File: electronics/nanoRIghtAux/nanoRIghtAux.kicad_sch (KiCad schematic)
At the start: 16 parts, among them J1 Conn_MM5451, J10 Conn_EA-GLCD, J11 Conn_MAX7219, J2 Conn_HYDA, J3 Conn_HYDB, J4 Conn_FUEL_FR, J5 Conn_FUEL_AL, J6 Conn_MOT_D, J7 Conn_MOT_C, J8 Conn_MOT_B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

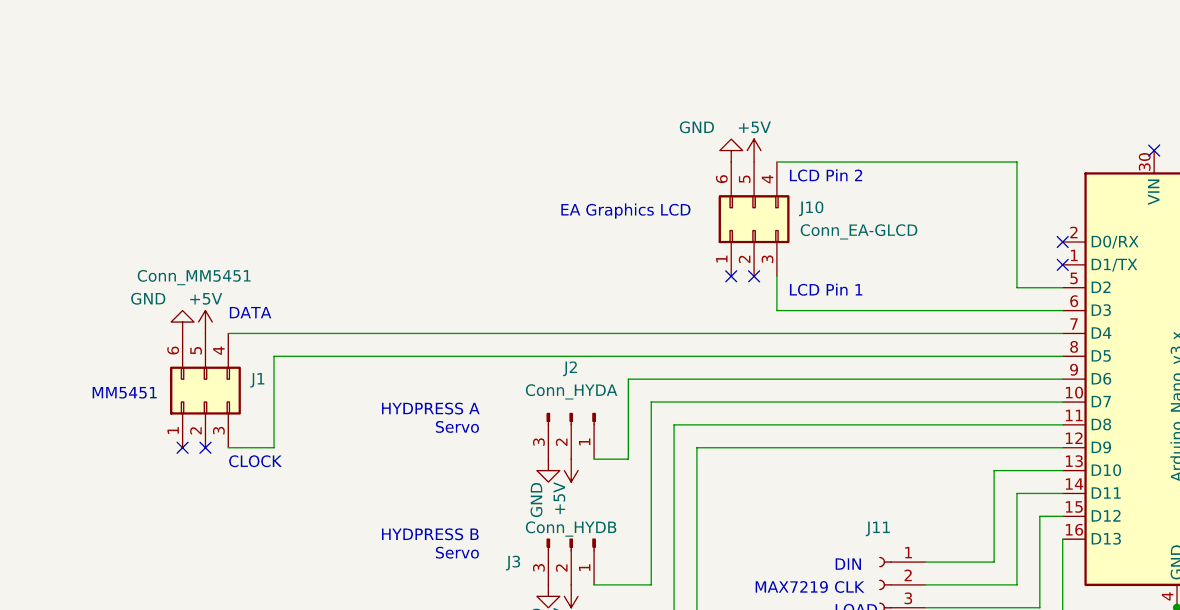
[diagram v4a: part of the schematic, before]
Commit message: changed 2x03 connector type
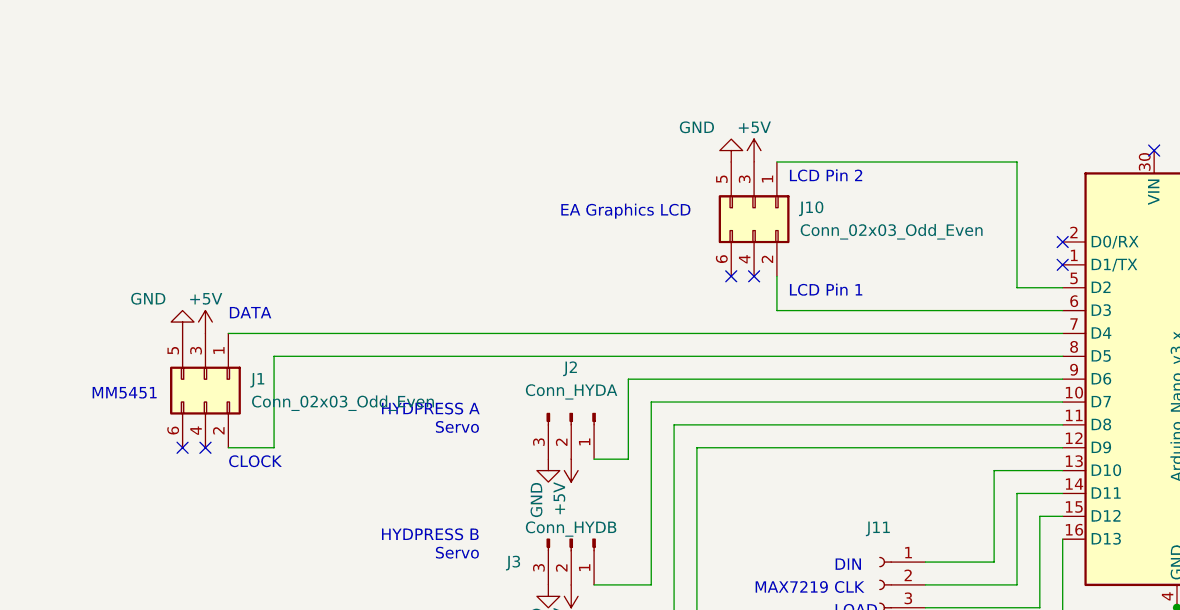
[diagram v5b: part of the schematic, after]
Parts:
- removed J1: Conn_MM5451, Connector_PinHeader_2.54mm:PinHeader_2x03_P2.54mm_Vertical, symbol Connector_Generic:Conn_02x03_Counter_Clockwise
- removed J10: Conn_EA-GLCD, Connector_PinHeader_2.54mm:PinHeader_2x03_P2.54mm_Vertical, symbol Connector_Generic:Conn_02x03_Counter_Clockwise
- added J1: Conn_02x03_Odd_Even, Connector_PinHeader_2.54mm:PinHeader_2x03_P2.54mm_Vertical, symbol Connector_Generic:Conn_02x03_Odd_Even
- added J10: Conn_02x03_Odd_Even, symbol Connector_Generic:Conn_02x03_Odd_Even
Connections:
- net +5V: now also J1.3 (Pin_3), J10.3 (Pin_3)
- net GND: now also J1.5 (Pin_5), J10.5 (Pin_5)
- net at A1.8 (D5): now also J1.2 (Pin_2)
- net at A1.7 (D4): now also J1.1 (Pin_1)
- net at A1.6 (D3): now also J10.2 (Pin_2)
- net at A1.5 (D2): now also J10.1 (Pin_1)

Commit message: PCB edit started
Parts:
- J1: value Conn_02x03_Odd_Even -> Conn_MM5451
- J10: value Conn_02x03_Odd_Even -> Conn_EA_GLCD; footprint (none) -> Connector_PinHeader_2.54mm:PinHeader_2x03_P2.54mm_Vertical
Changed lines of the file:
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@@
   )
   (symbol (lib_id "Connector_Generic:Conn_02x03_Odd_Even") (at 50.8 85.09 270) (unit 1)
-    (in_bom yes) (on_board yes) (dnp no) (fields_autoplaced)
+    (in_bom yes) (on_board yes) (dnp no)
     (property "Reference" "J1" (at 55.88 85.09 90)
       (effects (font (size 1.27 1.27)) (justify left))
     )
-    (property "Value" "Conn_02x03_Odd_Even" (at 55.88 87.63 90)
+    (property "Value" "Conn_MM5451" (at 33.02 83.82 90)
       (effects (font (size 1.27 1.27)) (justify left))
     )
@@
       (effects (font (size 1.27 1.27)) (justify left))
     )
-    (property "Value" "Conn_02x03_Odd_Even" (at 116.84 68.58 90)
+    (property "Value" "Conn_EA_GLCD" (at 116.84 68.58 90)
       (effects (font (size 1.27 1.27)) (justify left))
     )
-    (property "Footprint" "" (at 111.76 66.04 0)
+    (property "Footprint" "Connector_PinHeader_2.54mm:PinHeader_2x03_P2.54mm_Vertical" (at 111.76 66.04 0)
       (effects (font (size 1.27 1.27)) hide)
     )

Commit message: PWR input pinheader added, MAX7219_PWR pinheader added, PCB routing changed
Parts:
- added J12: Conn_PWRInput, Connector_PinHeader_2.54mm:PinHeader_1x02_P2.54mm_Vertical, symbol Connector:Conn_01x02_Pin
- added J13: Conn_MAX_Pwr, Connector_PinSocket_2.54mm:PinSocket_1x02_P2.54mm_Vertical, symbol Connector:Conn_01x02_Socket
- SW1, SW2, SW3: footprint Button_Switch_THT:SW_PUSH_6mm -> Connector_PinHeader_2.54mm:PinHeader_1x02_P2.54mm_Vertical
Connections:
- net +5V: now also J12.2 (Pin_2), J13.2 (Pin_2)
- net GND: now also J12.1 (Pin_1), J13.1 (Pin_1)
- net at J6.3 (Pin_3): now also U3.10 (Mot_D4); no longer U3.11 (Mot_D3)
- net at J6.4 (Pin_4): now also U3.11 (Mot_D3); no longer U3.10 (Mot_D4)
- net at J8.3 (Pin_3): now also U3.24 (Mot_B4); no longer U3.25 (Mot_B3)
- net at J8.4 (Pin_4): now also U3.25 (Mot_B3); no longer U3.24 (Mot_B4)
- net at J7.3 (Pin_3): now also U3.19 (Mot_C4); no longer U3.18 (Mot_C3)
- net at J7.4 (Pin_4): now also U3.18 (Mot_C3); no longer U3.19 (Mot_C4)
- net at J9.3 (Pin_3): now also U3.5 (Mot_A4); no longer U3.4 (Mot_A3)
- net at J9.4 (Pin_4): now also U3.4 (Mot_A3); no longer U3.5 (Mot_A4)
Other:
- moved on the sheet: J6, J7, J8, J9

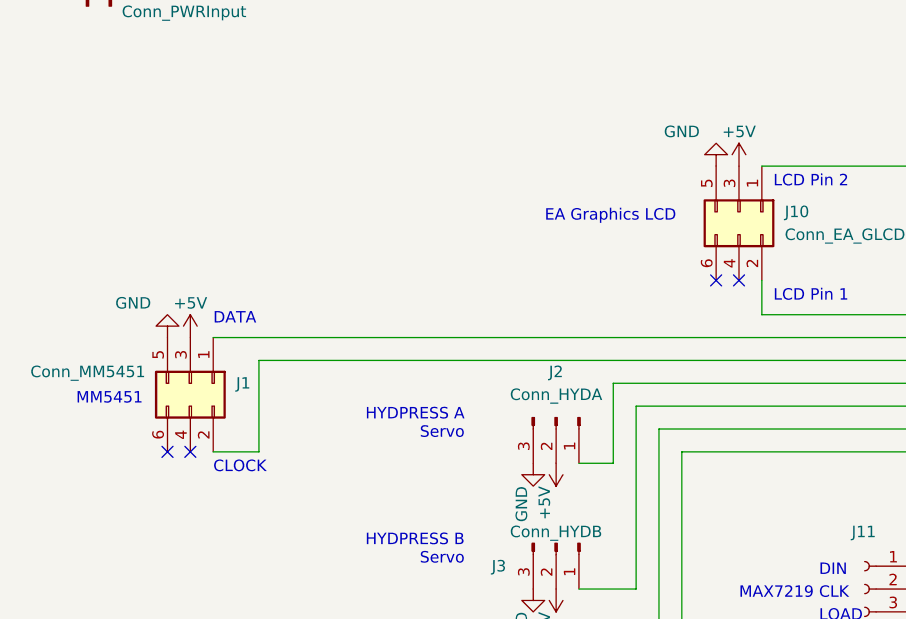
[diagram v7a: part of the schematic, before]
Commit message: first routing of TH components done.
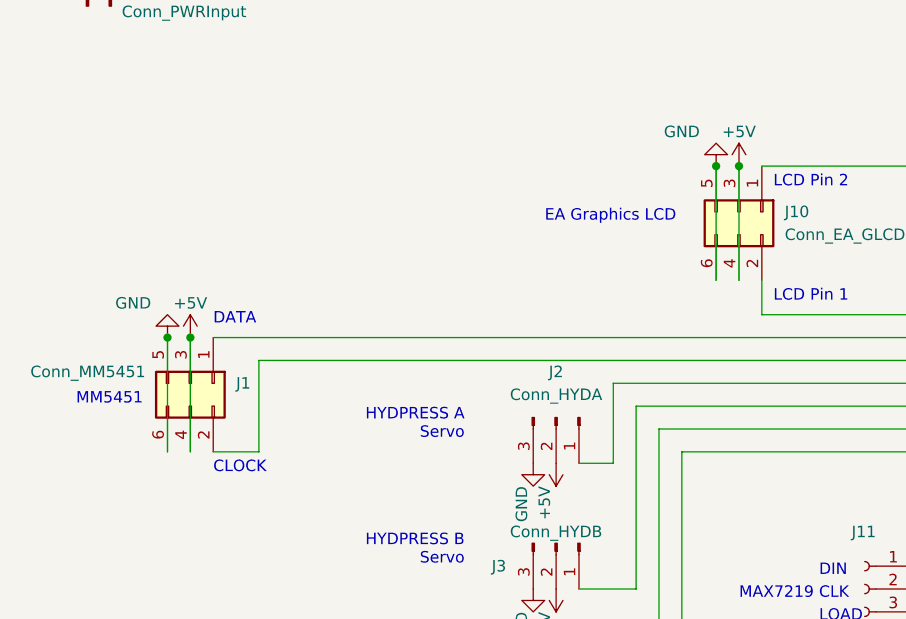
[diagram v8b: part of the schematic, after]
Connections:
- net +5V: now also J1.4 (Pin_4), J10.4 (Pin_4)
- net GND: now also J1.6 (Pin_6), J10.6 (Pin_6)
- no-connect marks 13 -> 9
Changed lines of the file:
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@@
   (junction (at 177.8 124.46) (diameter 0) (color 0 0 0 0)
   )
+  (junction (at 48.26 80.01) (diameter 0) (color 0 0 0 0)
+  )
   (junction (at 46.99 26.67) (diameter 0) (color 0 0 0 0)
   )
+  (junction (at 111.76 60.96) (diameter 0) (color 0 0 0 0)
+  )
+  (junction (at 50.8 80.01) (diameter 0) (color 0 0 0 0)
+  )
   (junction (at 158.75 110.49) (diameter 0) (color 0 0 0 0)
   )
   (junction (at 35.56 26.67) (diameter 0) (color 0 0 0 0)
   )
-  (no_connect (at 50.8 92.71))
+  (junction (at 109.22 60.96) (diameter 0) (color 0 0 0 0)
+  )
   (no_connect (at 163.83 59.69))
   (no_connect (at 156.21 59.69))
-  (no_connect (at 48.26 92.71))
   (no_connect (at 161.29 59.69))
   (no_connect (at 146.05 69.85))
-  (no_connect (at 109.22 73.66))
   (no_connect (at 171.45 80.01))
   (no_connect (at 146.05 72.39))
-  (no_connect (at 111.76 73.66))
   (no_connect (at 207.01 76.2))
   (no_connect (at 207.01 73.66))
@@
     (stroke (width 0) (type default))
   )
+  (wire (pts (xy 50.8 80.01) (xy 50.8 92.71))
+    (stroke (width 0) (type default))
+  )
   (wire (pts (xy 102.87 121.92) (xy 92.71 121.92))
     (stroke (width 0) (type default))
@@
     (stroke (width 0) (type default))
   )
+  (wire (pts (xy 48.26 80.01) (xy 48.26 92.71))
+    (stroke (width 0) (type default))
+  )
   (wire (pts (xy 105.41 92.71) (xy 105.41 139.7))
     (stroke (width 0) (type default))
@@
     (stroke (width 0) (type default))
   )
+  (wire (pts (xy 111.76 60.96) (xy 111.76 73.66))
+    (stroke (width 0) (type default))
+  )
   (wire (pts (xy 171.45 97.79) (xy 194.31 97.79))
     (stroke (width 0) (type default))
@@
     (stroke (width 0) (type default))
   )
+  (wire (pts (xy 109.22 60.96) (xy 109.22 73.66))
+    (stroke (width 0) (type default))
+  )
